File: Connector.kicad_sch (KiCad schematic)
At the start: 8 parts, among them J1 Conn_01x04_Socket, J2 Conn_01x04_Socket, U3 TPS7A20xxxDBV, U4 TPS7A20xxxDBV

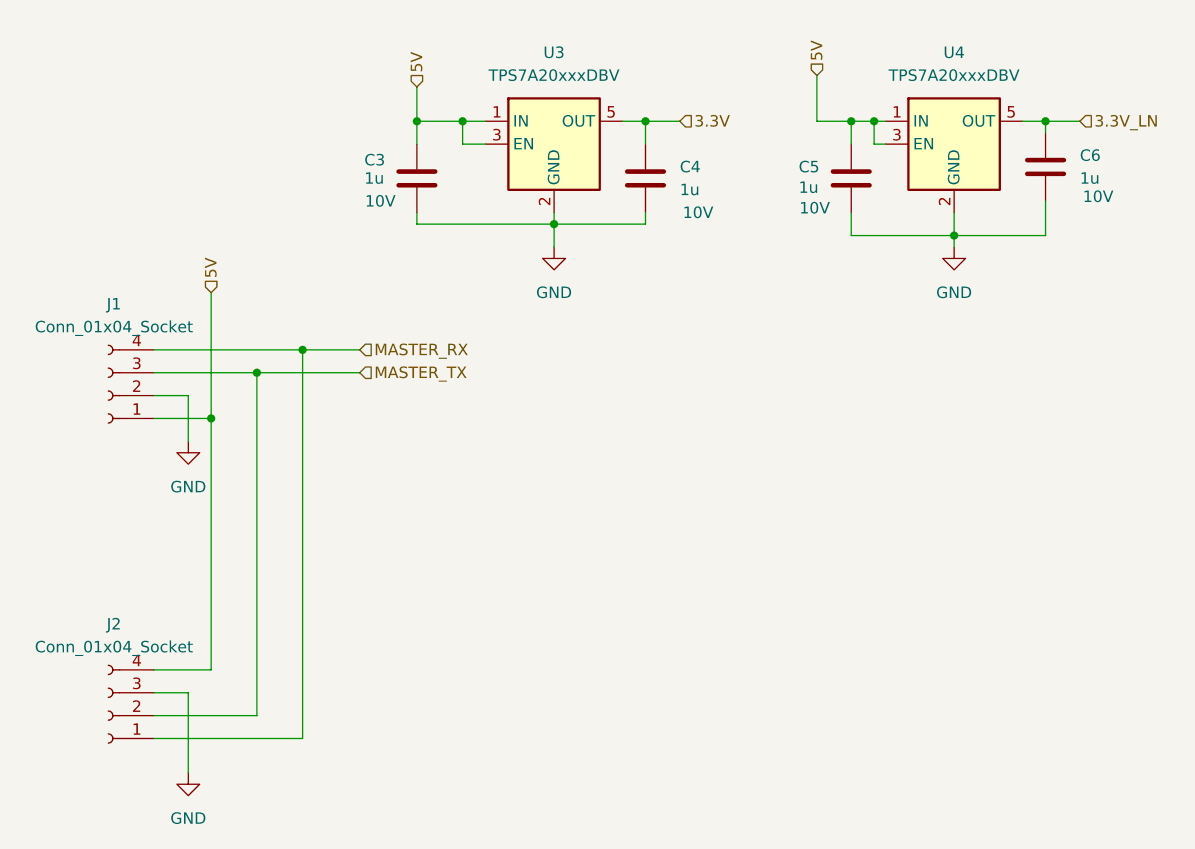
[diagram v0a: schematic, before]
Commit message: rule-check: Fix the ERC errors and warnings
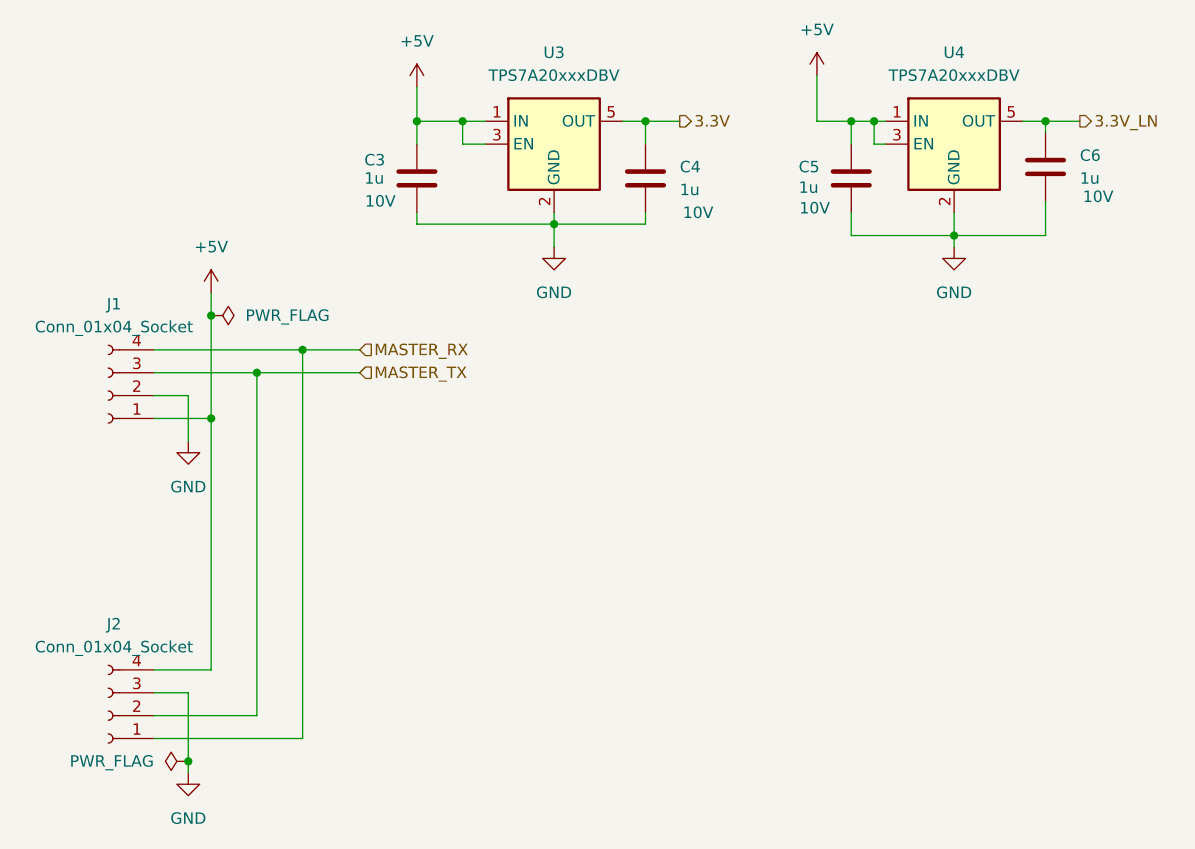
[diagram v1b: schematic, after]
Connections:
- net 5V renamed +5V
